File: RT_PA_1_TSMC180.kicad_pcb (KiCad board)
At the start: 4 copper layers, 160 x 100 mm, 120 parts, among them J1 Conn_Coaxial, J10 Conn_01x01, J101 Conn_01x01, J11 Conn_01x01, J12 Conn_01x01, J13 Conn_01x01, J14 Conn_01x01_Female, J15 Conn_01x01_Female, J16 Conn_01x01, J171 Conn_01x01, J172 Conn_01x01, J173 Conn_01x01, J18 Conn_01x01, J19 Conn_01x01, J2 Conn_01x01, J20 Conn_01x01, J201 Conn_01x01, J202 Conn_01x01, J203 Conn_01x01, J22 Conn_01x01, J25 Conn_01x01, J27 Conn_01x01, J28 Conn_01x01, J29 Conn_Coaxial, J3 Conn_Coaxial, J31 Conn_Coaxial, J33 Conn_Coaxial, J35 Conn_Coaxial, J37 Conn_Coaxial, J39 Conn_Coaxial, J4 Conn_01x01, J401 Conn_01x02, J402 Conn_01x01, J41 Conn_Coaxial, J42 Conn_01x01, J43 Conn_Coaxial, J44 Conn_01x01, J45 Conn_01x01, J46 Conn_01x01, J47 Conn_01x01, J48 Conn_01x01, J49 Conn_01x04, J5 Conn_Coaxial, J50 Conn_01x04, J51 Conn_01x01, J52 Conn_01x01, J53 Conn_01x01, J54 Conn_01x01, J55 Conn_01x02, J56 Conn_01x02, J57 Conn_01x02, J58 Conn_01x03, J6 Conn_01x01, J60 Conn_01x01, J61 Conn_01x02, J62 Conn_01x03, J63 Conn_01x01, J64 Conn_01x01, J65 Conn_Coaxial, J66 Conn_01x01, J67 Conn_Coaxial, J7 Conn_Coaxial, J8 Conn_01x01, J9 Conn_01x01_Female, U1 PART1p68

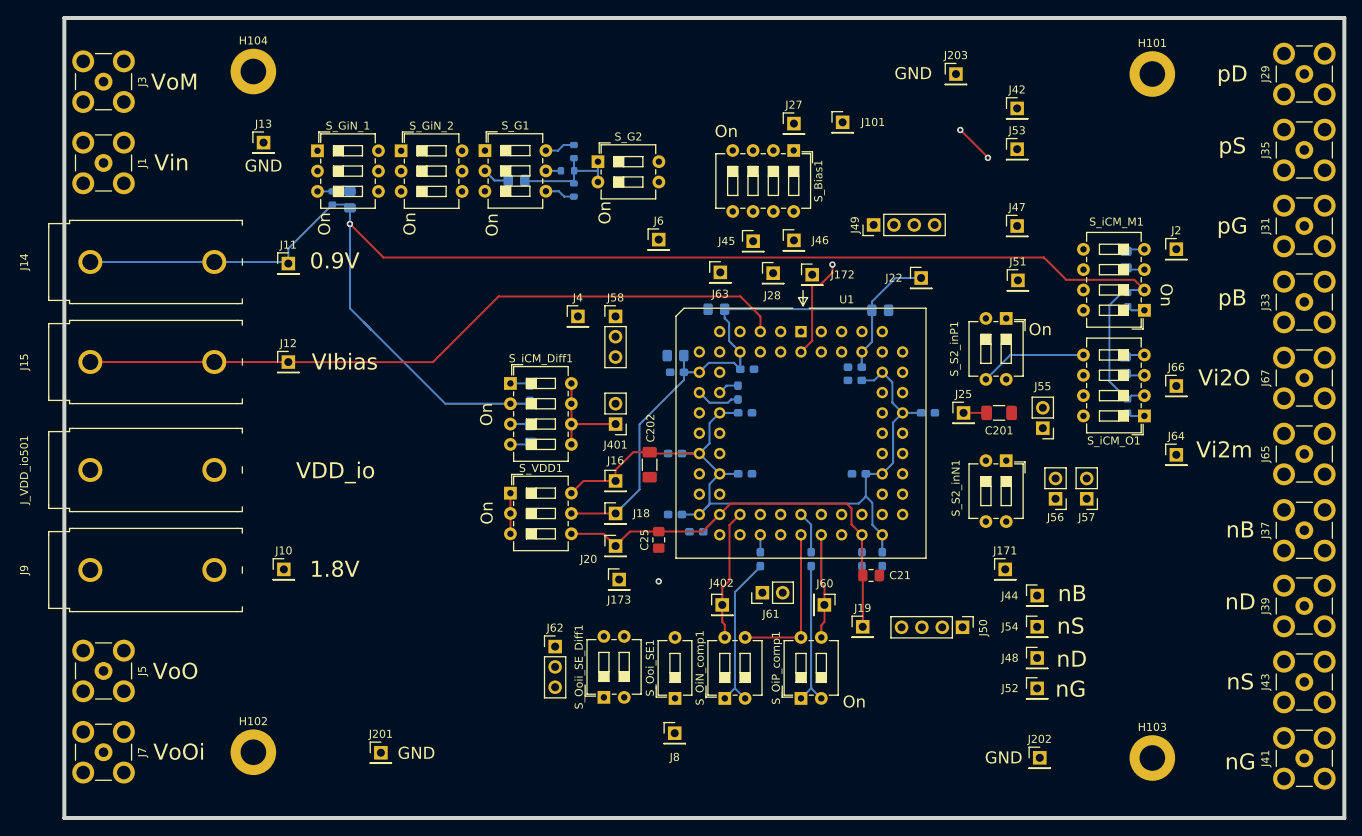
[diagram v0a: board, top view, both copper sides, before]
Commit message: Some cleanup and reversed On marker for switchs
Signed-off-by: Alexis Jeandet <alexis.jeandet@member.fsf.org>
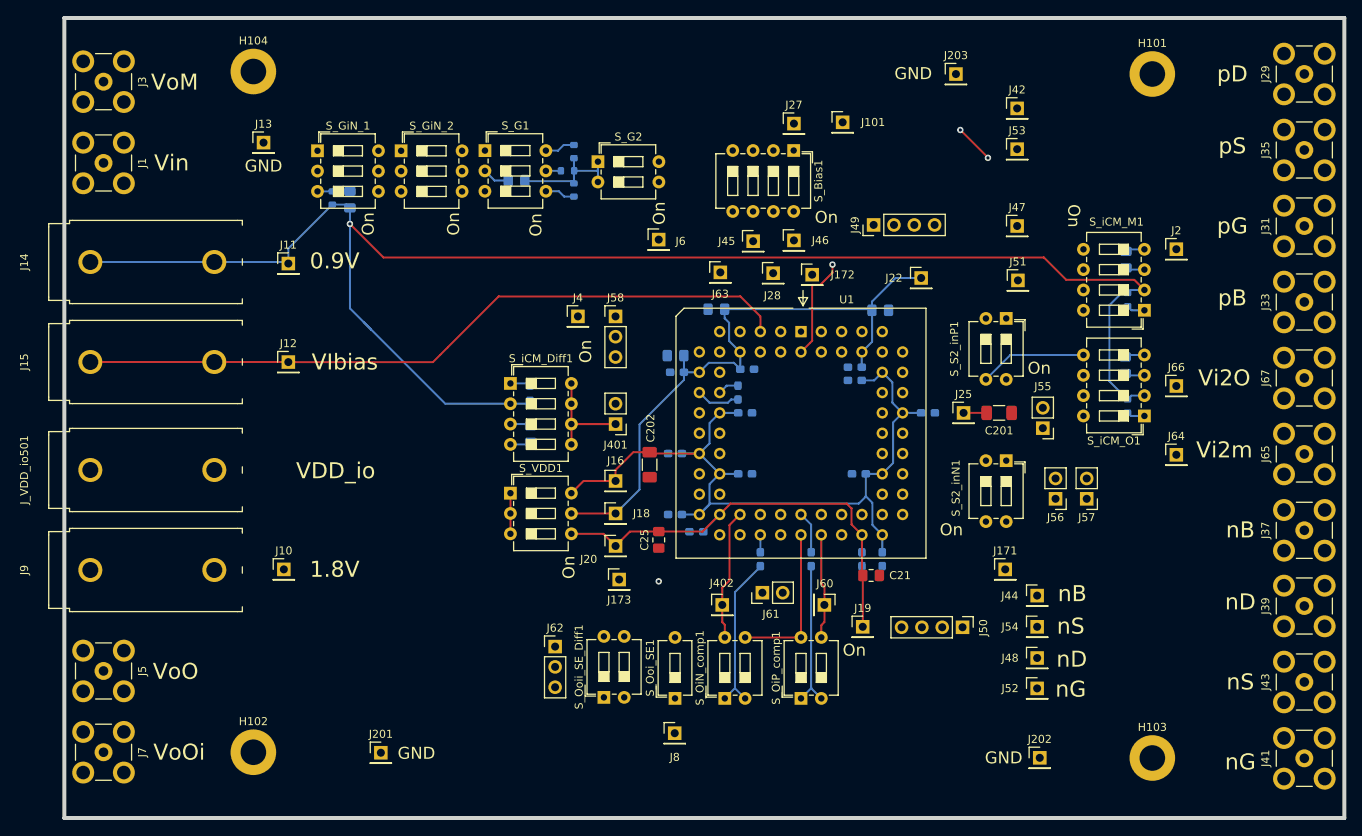
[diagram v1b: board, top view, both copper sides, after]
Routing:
- net /Vo1O: track 28.1 -> 13.1 mm
- net /Vo2O: track 31.2 -> 16.4 mm

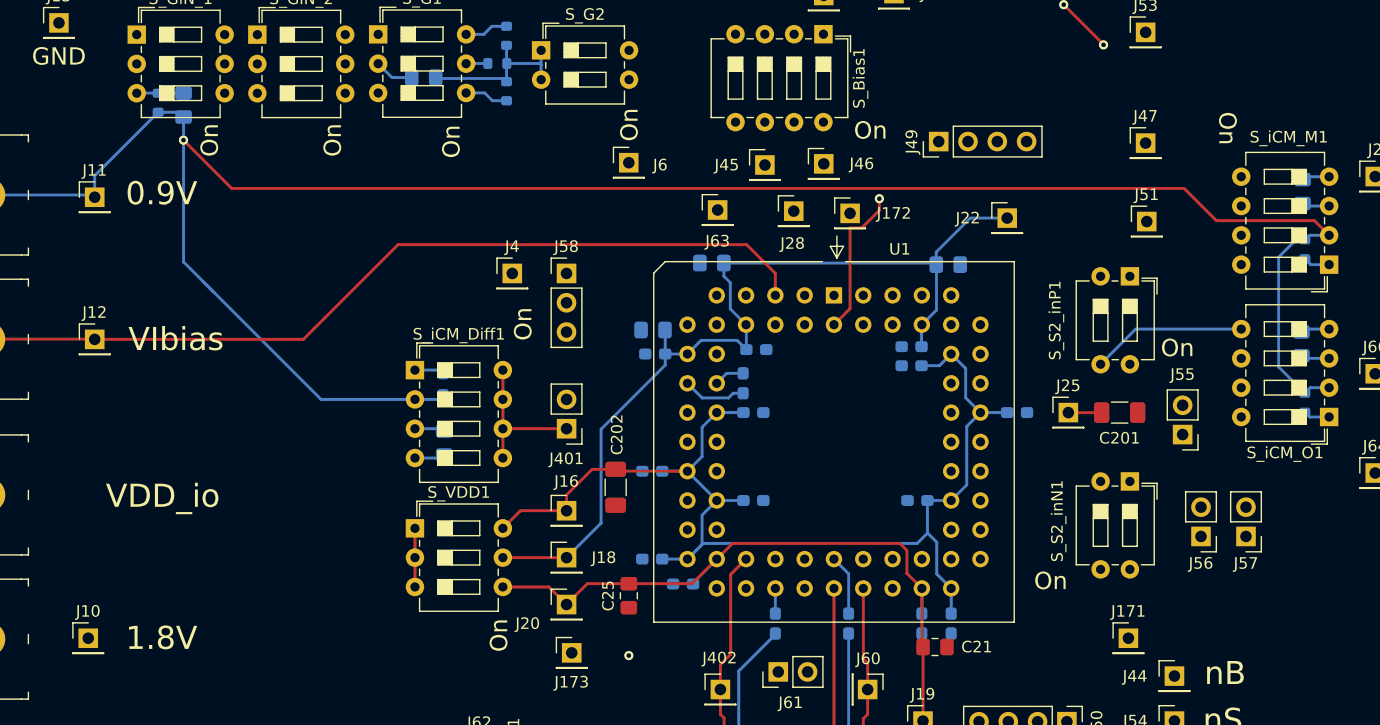
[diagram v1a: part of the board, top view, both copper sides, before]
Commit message: Adds some legned and one testpoint for VDD_io
Signed-off-by: Alexis Jeandet <alexis.jeandet@member.fsf.org>
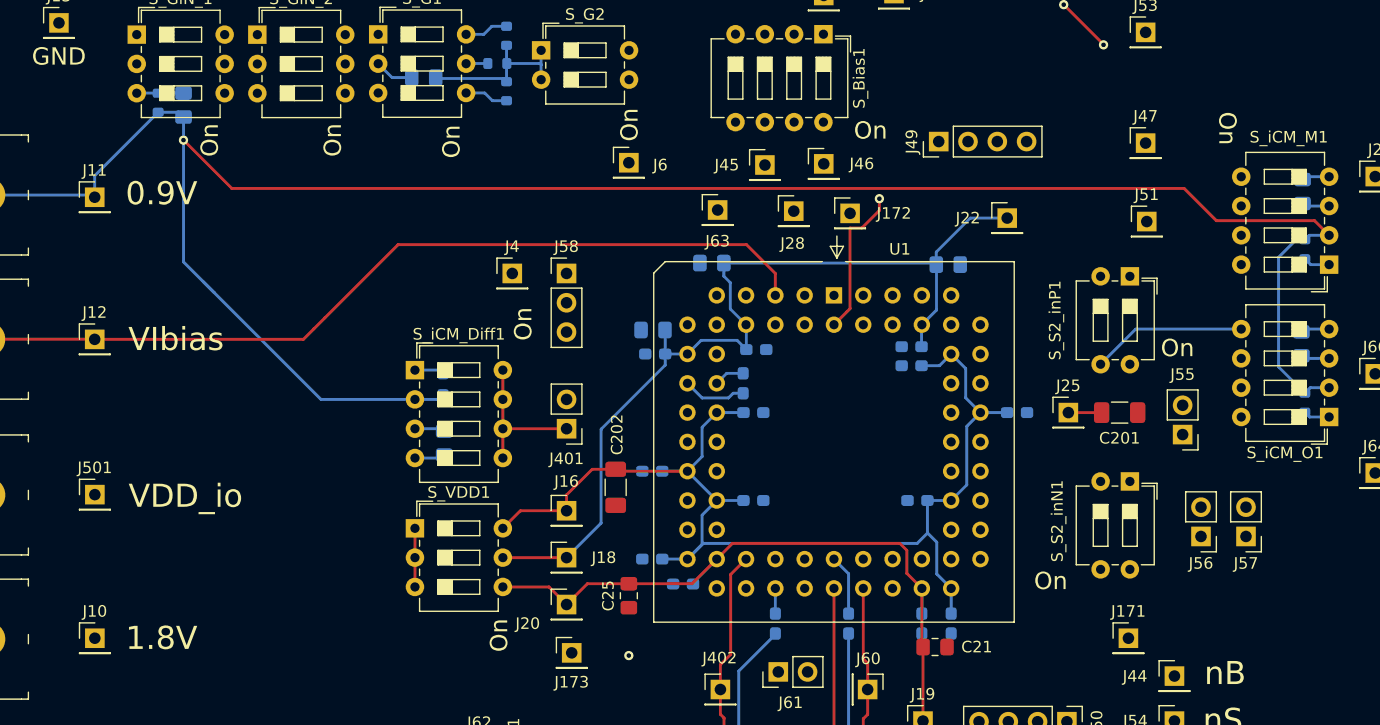
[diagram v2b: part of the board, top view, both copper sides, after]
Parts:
- added J501: Conn_01x01, Connector_PinHeader_2.54mm:PinHeader_1x01_P2.54mm_Vertical, F.Cu at (92.0, 109.5)
- moved J10 0.57 mm to (92.0, 121.9)
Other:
- board text added: "GND_io"

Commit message: PCB updated ready for review
Signed-off-by: Alexis Jeandet <alexis.jeandet@member.fsf.org>
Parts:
- added J204: Conn_01x01_Female, banana:Banana_test_point_4mm, F.Cu at (75.1, 102.8)
- moved J63 58.0 mm to (152.3, 142.4)
- moved J101 20.4 mm to (153.9, 85.1)
- moved J27 11.6 mm to (166.8, 66.2)
- moved J45 11.6 mm to (161.7, 80.9)
- moved J46 11.6 mm to (166.8, 80.8)
- moved S_Bias1 11.6 mm to (166.7, 69.6)
- moved J51 10.6 mm to (178.1, 76.5)
- moved J49 10.4 mm to (154.9, 80.9), turned to 270 degrees
- moved C11 9.65 mm to (147.4, 87.4), turned to 180 degrees
- moved C19 9.38 mm to (164.9, 87.5), turned to 0 degrees
- moved J28 8.76 mm to (161.4, 85.1)
- moved J47 8.13 mm to (178.1, 72.6)
- moved J501 5.08 mm to (92.0, 114.6)
- moved J_VDD_io501 5.05 mm to (75.1, 114.6)
- moved J53 5.03 mm to (178.1, 68.7)
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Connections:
- U1 pad 1: /VM_M -> /Vo1m
- U1 pad 2: /Vo1m -> /VM_M
- U1 pad 3: /VbiasO -> /pS
- U1 pad 4: /VbiasDiff -> /pB
- U1 pad 5: /VIbias -> /pG
- U1 pad 6: /VbiasM -> /pD
- U1 pad 63: GND -> /VDD_M
- U1 pad 64: /VDD_M -> GND
- U1 pad 65: /pD -> /VbiasM
- U1 pad 66: /pG -> /VIbias
- U1 pad 67: /pB -> /VbiasDiff
- U1 pad 68: /pS -> /VbiasO
- U1 pad 7: GND -> /VDD_M
- U1 pad 8: /VDD_M -> GND
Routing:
- net /pG: track 67.0 -> 93.0 mm
- net /Vo1m: track 30.8 -> 8.03 mm, vias 1 -> 0
- net /pD: track 75.9 -> 95.9 mm
- net /pB: track 72.4 -> 91.4 mm
- net /VIbias: track 124.3 -> 138.2 mm
- net /VoM: track 125.0 -> 114.2 mm
- net /Vbi: track 75.2 -> 84.0 mm
- net /VDD_M: track 79.6 -> 72.5 mm
- net /pS: track 79.6 -> 85.2 mm
- net /0V9_g: track 202.7 -> 197.2 mm, vias 1 -> 0
- net /VbiasO: track 15.7 -> 20.9 mm
- net /VM_M: track 7.69 -> 10.3 mm
- net /1V8_g: track 59.2 -> 61.2 mm
- net /VDD_io: track 103.2 -> 105.2 mm
- net /VbiasM: track 18.2 -> 16.3 mm
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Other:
- board text added: "RT_PA_1_TSMC180 V2.0"
